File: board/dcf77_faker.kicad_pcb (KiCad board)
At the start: 4 copper layers, 69 x 32 mm, 46 parts, among them J1 Barrel_Jack, J2 DBG, J3 ANT, J4 LCD_I2C, SW1 RST, U1 NCP1117ST33T3G, U2 ATSAML21G18B-AUT, X1 32.768kHz, X2 31MHz

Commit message: board: align schematic to grid
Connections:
- U2 pad 2: /XOUT32 -> unconnected-(U2-Pad2)
- U2 pad 24: /XOUT -> unconnected-(U2-Pad24)

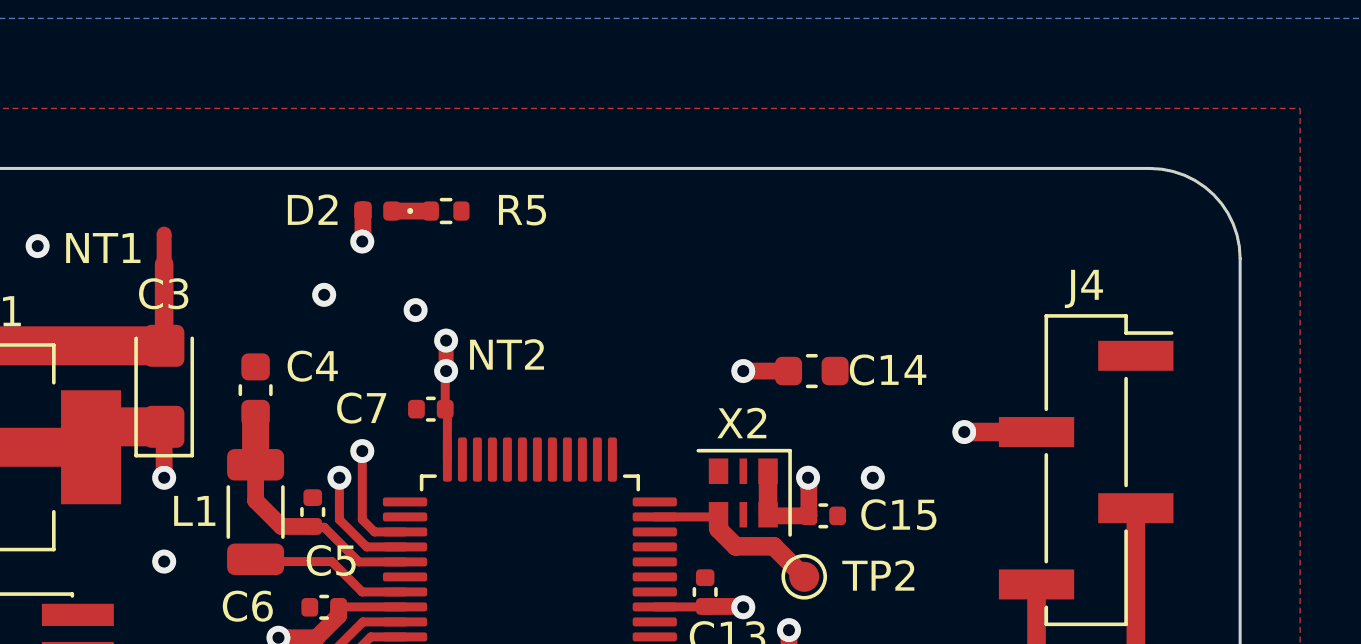
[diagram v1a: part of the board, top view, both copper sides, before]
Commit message: board: add buttons to set hour/minute or reset second
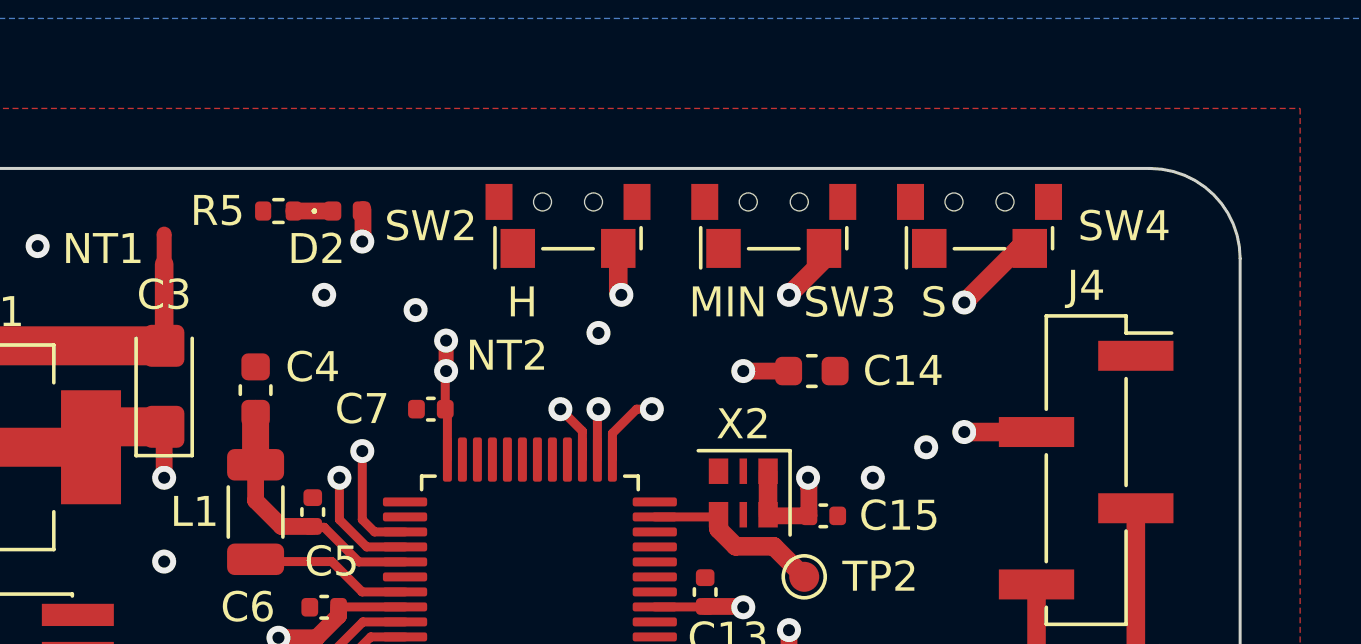
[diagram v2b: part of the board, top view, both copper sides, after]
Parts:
- added SW2: H, Button_Switch_SMD_Side:Shou_Han_TS24CA, F.Cu at (196.6, 58.2)
- added SW3: MIN, Button_Switch_SMD_Side:Shou_Han_TS24CA, F.Cu at (203.5, 58.2)
- added SW4: S, Button_Switch_SMD_Side:Shou_Han_TS24CA, F.Cu at (210.3, 58.2)
- SW1: footprint Button_Switch_SMD_Custom:Shou_Han_TS24CA -> Button_Switch_SMD_Side:Shou_Han_TS24CA
- moved R5 5.59 mm to (186.9, 58.4), turned to 0 degrees
- moved D2 1.02 mm to (189.2, 58.4), turned to 0 degrees
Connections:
- net /VDDIO1 renamed /VDDIO2
- U2 pad 25: unconnected-(U2-Pad25) -> /H
- U2 pad 26: unconnected-(U2-Pad26) -> /MIN
- U2 pad 27: unconnected-(U2-Pad27) -> /S
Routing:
- net /S: track 0.00 -> 23.3 mm, vias 0 -> 3
- net /MIN: track 0.00 -> 13.1 mm, vias 0 -> 3
- net /H: track 0.00 -> 8.34 mm, vias 0 -> 2

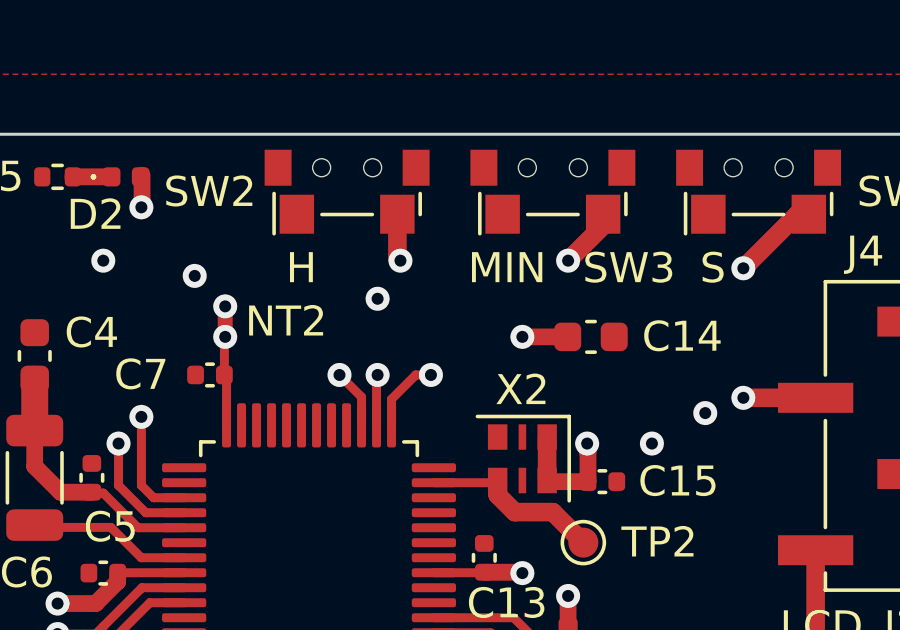
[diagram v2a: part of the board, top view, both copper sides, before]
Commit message: board: reorder HMS button pins
this increases planarity of the PCB tracks
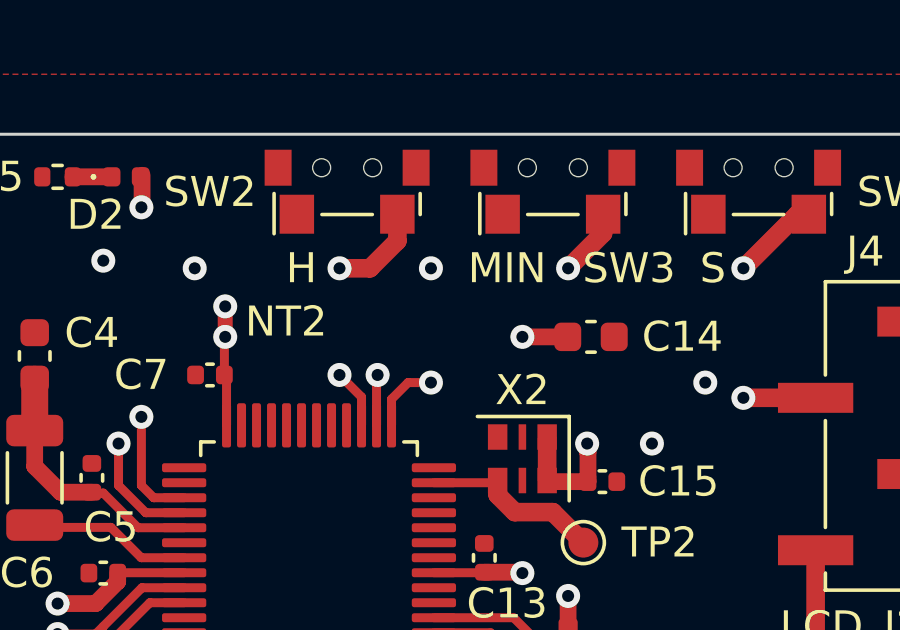
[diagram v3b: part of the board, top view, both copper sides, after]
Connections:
- U2 pad 25: /H -> /S
- U2 pad 27: /S -> /H
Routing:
- net /S: track 23.3 -> 18.6 mm
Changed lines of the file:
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@@
   (net 19 "unconnected-(J2-Pad8)")
   (net 20 "unconnected-(J2-Pad9)")
-  (net 21 "Net-(R4-Pad1)")
-  (net 22 "Net-(SW1-Pad2)")
+  (net 21 "Net-(J3-Pad1)")
+  (net 22 "Net-(R2-Pad2)")
   (net 23 "/TCC0WO0")
   (net 24 "/XIN")
@@
       (net 1 "GND") (pinfunction "1") (pintype "passive"))
     (pad "2" smd rect (at 1.675 1.5 180) (size 1.15 1.3) (layers "F.Cu" "F.Paste" "F.Mask")
-      (net 22 "Net-(SW1-Pad2)") (pinfunction "2") (pintype "passive"))
+      (net 22 "Net-(R2-Pad2)") (pinfunction "2") (pintype "passive"))
     (pad "3" smd rect (at 2.3 -0.05 180) (size 0.9 1.2) (layers "F.Cu" "F.Paste" "F.Mask"))
     (pad "3" smd rect (at -2.3 -0.05 180) (size 0.9 1.2) (layers "F.Cu" "F.Paste" "F.Mask"))
@@
       (net 10 "/~{RST}") (pintype "passive"))
     (pad "2" smd roundrect (at 0.51 0 270) (size 0.54 0.64) (layers "F.Cu" "F.Paste" "F.Mask") (roundrect_rratio 0.25)
-      (net 22 "Net-(SW1-Pad2)") (pintype "passive"))
+      (net 22 "Net-(R2-Pad2)") (pintype "passive"))
     (model "${KICAD6_3DMODEL_DIR}/Resistor_SMD.3dshapes/R_0402_1005Metric.wrl"
       (offset (xyz 0 0 0))
@@
       (net 38 "unconnected-(U2-Pad24)") (pinfunction "PA15") (pintype "bidirectional+no_connect"))
     (pad "25" smd roundrect (at 4.1625 2.75 90) (size 1.475 0.3) (layers "F.Cu" "F.Paste" "F.Mask") (roundrect_rratio 0.25)
-      (net 51 "/H") (pinfunction "PA16") (pintype "bidirectional"))
+      (net 53 "/S") (pinfunction "PA16") (pintype "bidirectional"))
     (pad "26" smd roundrect (at 4.1625 2.25 90) (size 1.475 0.3) (layers "F.Cu" "F.Paste" "F.Mask") (roundrect_rratio 0.25)
       (net 52 "/MIN") (pinfunction "PA17") (pintype "bidirectional"))
     (pad "27" smd roundrect (at 4.1625 1.75 90) (size 1.475 0.3) (layers "F.Cu" "F.Paste" "F.Mask") (roundrect_rratio 0.25)
-      (net 53 "/S") (pinfunction "PA18") (pintype "bidirectional"))
+      (net 51 "/H") (pinfunction "PA18") (pintype "bidirectional"))
     (pad "28" smd roundrect (at 4.1625 1.25 90) (size 1.475 0.3) (layers "F.Cu" "F.Paste" "F.Mask") (roundrect_rratio 0.25)
       (net 39 "unconnected-(U2-Pad28)") (pinfunction "PA19") (pintype "bidirectional+no_connect"))
@@
     (fp_line (start -0.525 0.27) (end -0.525 -0.27) (layer "F.Fab") (width 0.1))
     (pad "1" smd roundrect (at -0.51 0) (size 0.54 0.64) (layers "F.Cu" "F.Paste" "F.Mask") (roundrect_rratio 0.25)
-      (net 21 "Net-(R4-Pad1)") (pintype "passive"))
+      (net 21 "Net-(J3-Pad1)") (pintype "passive"))
     (pad "2" smd roundrect (at 0.51 0) (size 0.54 0.64) (layers "F.Cu" "F.Paste" "F.Mask") (roundrect_rratio 0.25)
       (net 23 "/TCC0WO0") (pintype "passive"))
@@
     (fp_line (start -2.54 1.59) (end -1.27 1.59) (layer "F.Fab") (width 0.1))
     (pad "1" smd rect (at 1.655 -1.27 270) (size 2.51 1) (layers "F.Cu" "F.Paste" "F.Mask")
-      (net 21 "Net-(R4-Pad1)") (pinfunction "Pin_1") (pintype "passive"))
+      (net 21 "Net-(J3-Pad1)") (pinfunction "Pin_1") (pintype "passive"))
     (pad "2" smd rect (at -1.655 1.27 270) (size 2.51 1) (layers "F.Cu" "F.Paste" "F.Mask")
       (net 1 "GND") (pinfunction "Pin_2") (pintype "passive"))
@@
   (segment (start 196.215 77.089) (end 197.104 77.978) (width 0.620014) (layer "F.Cu") (net 1))
   (segment (start 193.767 77.034) (end 193.857 77.034) (width 0.299974) (layer "F.Cu") (net 1))
-  (via (at 191.516 61.722) (size 0.8) (drill 0.4) (layers "F.Cu" "B.Cu") (free) (net 1))
+  (via (at 191.516 61.468) (size 0.8) (drill 0.4) (layers "F.Cu" "B.Cu") (free) (net 1))
   (via (at 178.9176 59.5884) (size 0.8) (drill 0.4) (layers "F.Cu" "B.Cu") (free) (net 1))
   (via (at 206.756 67.31) (size 0.8) (drill 0.4) (layers "F.Cu" "B.Cu") (free) (net 1))
@@
   (segment (start 187.452 72.644) (end 188.214 73.406) (width 0.620014) (layer "In1.Cu") (net 48))
   (segment (start 200.152 82.55) (end 188.214 82.55) (width 0.620014) (layer "In2.Cu") (net 48))
-  (segment (start 198.076 65.83) (end 198.882 65.024) (width 0.299974) (layer "F.Cu") (net 51))
-  (segment (start 198.076 66.7035) (end 198.076 65.83) (width 0.299974) (layer "F.Cu") (net 51))
-  (segment (start 198.271 61.111) (end 198.374 61.214) (width 0.620014) (layer "F.Cu") (net 51))
-  (segment (start 198.271 59.666) (end 198.271 61.111) (width 0.620014) (layer "F.Cu") (net 51))
-  (segment (start 198.882 65.024) (end 199.39 65.024) (width 0.299974) (layer "F.Cu") (net 51))
-  (via (at 198.374 61.214) (size 0.8) (drill 0.4) (layers "F.Cu" "B.Cu") (net 51))
-  (via (at 199.39 65.024) (size 0.8) (drill 0.4) (layers "F.Cu" "B.Cu") (net 51))
-  (segment (start 199.39 65.024) (end 199.39 62.23) (width 0.56007) (layer "In1.Cu") (net 51))
-  (segment (start 199.39 62.23) (end 198.374 61.214) (width 0.56007) (layer "In1.Cu") (net 51))
-  (segment (start 205.129 59.666) (end 205.129 60.047) (width 0.620014) (layer "F.Cu") (net 52))
+  (segment (start 198.271 59.666) (end 198.271 60.555) (width 0.620014) (layer "F.Cu") (net 51))
+  (segment (start 197.076 66.7035) (end 197.076 65.758) (width 0.299974) (layer "F.Cu") (net 51))
+  (segment (start 197.076 65.758) (end 196.342 65.024) (width 0.299974) (layer "F.Cu") (net 51))
+  (segment (start 198.271 60.555) (end 197.358 61.468) (width 0.620014) (layer "F.Cu") (net 51))
+  (segment (start 197.358 61.468) (end 196.342 61.468) (width 0.620014) (layer "F.Cu") (net 51))
+  (via (at 196.342 65.024) (size 0.8) (drill 0.4) (layers "F.Cu" "B.Cu") (net 51))
+  (via (at 196.342 61.468) (size 0.8) (drill 0.4) (layers "F.Cu" "B.Cu") (net 51))
+  (segment (start 196.342 65.024) (end 196.342 61.468) (width 0.620014) (layer "In1.Cu") (net 51))
+  (segment (start 205.129 59.666) (end 205.129 60.301) (width 0.620014) (layer "F.Cu") (net 52))
   (segment (start 197.576 65.06) (end 197.612 65.024) (width 0.299974) (layer "F.Cu") (net 52))
   (segment (start 197.576 66.7035) (end 197.576 65.06) (width 0.299974) (layer "F.Cu") (net 52))
-  (segment (start 205.129 60.047) (end 203.962 61.214) (width 0.620014) (layer "F.Cu") (net 52))
-  (via (at 203.962 61.214) (size 0.8) (drill 0.4) (layers "F.Cu" "B.Cu") (net 52))
-  (via (at 197.612 62.484) (size 0.8) (drill 0.4) (layers "F.Cu" "B.Cu") (net 52))
+  (segment (start 205.129 60.301) (end 203.962 61.468) (width 0.620014) (layer "F.Cu") (net 52))
+  (via (at 203.962 61.468) (size 0.8) (drill 0.4) (layers "F.Cu" "B.Cu") (net 52))
+  (via (at 199.39 61.468) (size 0.8) (drill 0.4) (layers "F.Cu" "B.Cu") (net 52))
   (via (at 197.612 65.024) (size 0.8) (drill 0.4) (layers "F.Cu" "B.Cu") (net 52))
-  (segment (start 197.612 65.024) (end 197.612 62.484) (width 0.56007) (layer "In1.Cu") (net 52))
-  (segment (start 197.612 62.484) (end 202.692 62.484) (width 0.56007) (layer "In2.Cu") (net 52))
-  (segment (start 202.692 62.484) (end 203.962 61.214) (width 0.56007) (layer "In2.Cu") (net 52))
+  (segment (start 197.612 65.024) (end 197.612 63.246) (width 0.620014) (layer "In1.Cu") (net 52))
+  (segment (start 197.612 63.246) (end 199.39 61.468) (width 0.620014) (layer "In1.Cu") (net 52))
+  (segment (start 199.39 61.468) (end 203.962 61.468) (width 0.620014) (layer "In2.Cu") (net 52))
   (segment (start 211.606 59.666) (end 209.804 61.468) (width 0.620014) (layer "F.Cu") (net 53))
   (segment (start 211.987 59.666) (end 211.606 59.666) (width 0.620014) (layer "F.Cu") (net 53))
-  (segment (start 197.076 66.7035) (end 197.076 65.758) (width 0.299974) (layer "F.Cu") (net 53))
-  (segment (start 197.076 65.758) (end 196.342 65.024) (width 0.299974) (layer "F.Cu") (net 53))
-  (via (at 208.534 66.294) (size 0.8) (drill 0.4) (layers "F.Cu" "B.Cu") (net 53))
-  (via (at 196.342 65.024) (size 0.8) (drill 0.4) (layers "F.Cu" "B.Cu") (net 53))
+  (segment (start 198.076 66.7035) (end 198.076 65.83) (width 0.299974) (layer "F.Cu") (net 53))
+  (segment (start 198.076 65.83) (end 198.628 65.278) (width 0.299974) (layer "F.Cu") (net 53))
+  (segment (start 198.628 65.278) (end 199.39 65.278) (width 0.299974) (layer "F.Cu") (net 53))
+  (via (at 208.534 65.278) (size 0.8) (drill 0.4) (layers "F.Cu" "B.Cu") (net 53))
+  (via (at 199.39 65.278) (size 0.8) (drill 0.4) (layers "F.Cu" "B.Cu") (net 53))
   (via (at 209.804 61.468) (size 0.8) (drill 0.4) (layers "F.Cu" "B.Cu") (net 53))
-  (segment (start 208.534 66.294) (end 208.534 62.738) (width 0.620014) (layer "In1.Cu") (net 53))
   (segment (start 208.534 62.738) (end 209.804 61.468) (width 0.620014) (layer "In1.Cu") (net 53))
-  (segment (start 196.342 65.024) (end 196.342 65.532) (width 0.56007) (layer "In2.Cu") (net 53))
-  (segment (start 196.342 65.532) (end 197.104 66.294) (width 0.56007) (layer "In2.Cu") (net 53))
-  (segment (start 197.104 66.294) (end 208.534 66.294) (width 0.56007) (layer "In2.Cu") (net 53))
+  (segment (start 208.534 62.738) (end 208.534 65.024) (width 0.620014) (layer "In1.Cu") (net 53))
+  (segment (start 199.39 65.278) (end 208.534 65.278) (width 0.620014) (layer "In2.Cu") (net 53))
   (segment (start 199.4885 71.616) (end 201.156 71.616) (width 0.299974) (layer "F.Cu") (net 54))
   (segment (start 192.504 65.024) (end 192.504 63.782) (width 0.299974) (layer "F.Cu") (net 54))

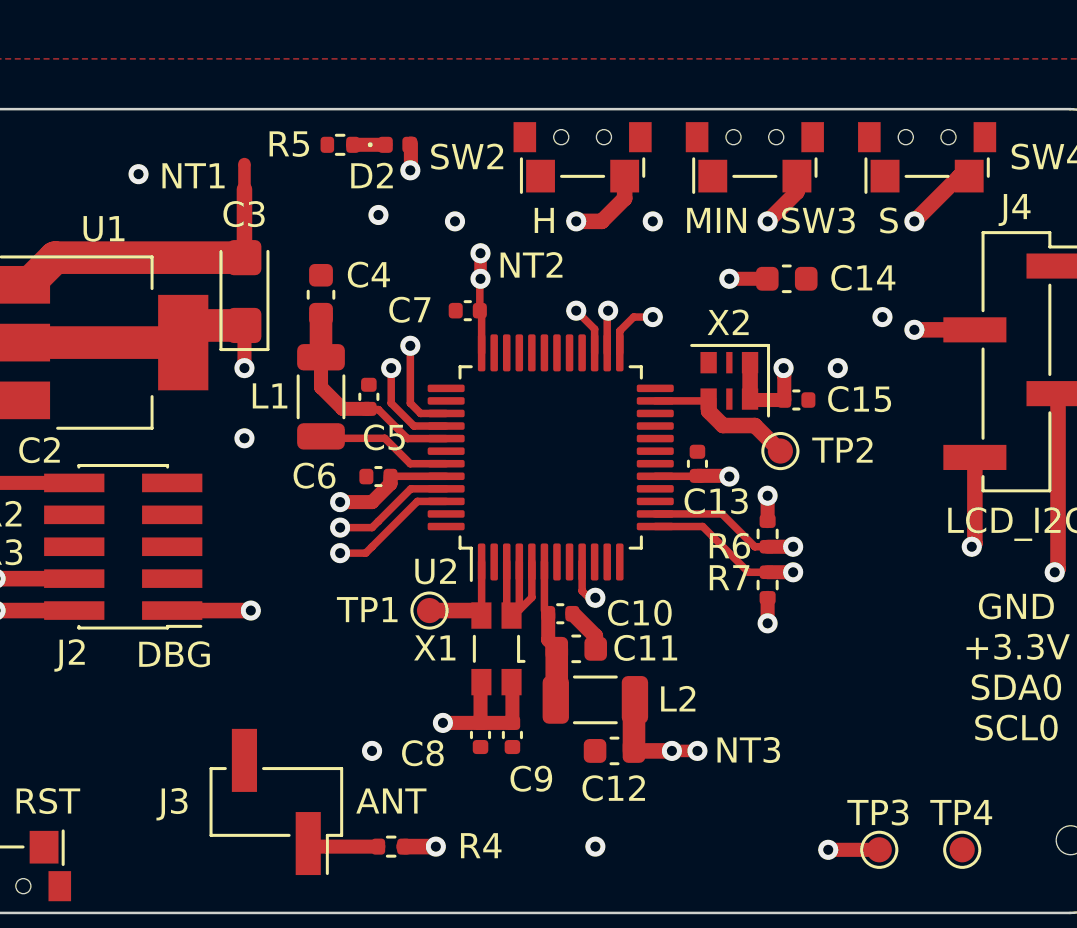
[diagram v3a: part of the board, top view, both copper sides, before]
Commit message: board: force VDDIO1 and VDDIO2 to be independent nets
otherwise the name of the common net will keep changing
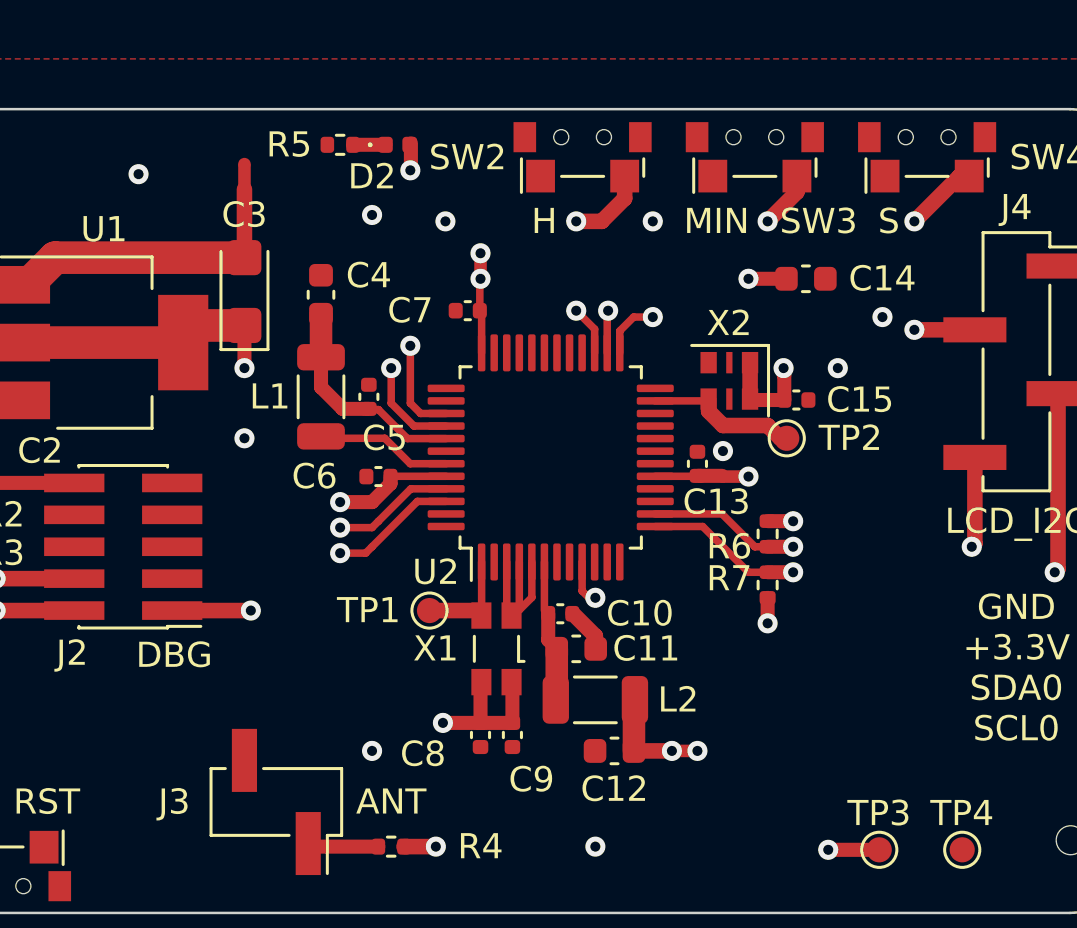
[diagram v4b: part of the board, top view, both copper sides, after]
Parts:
- added NT4: NetTie_2, NetTie:NetTie-2_SMD_Pad0.5mm, F.Cu at (202.7, 71.6)
- moved C14 0.76 mm to (205.5, 63.8)
- moved TP2 0.57 mm to (204.7, 70.1)
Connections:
- C13 pad 1: /VDDIO2 -> /VDDIO1
- U2 pad 17: /VDDIO2 -> /VDDIO1
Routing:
- net /VDDIO1: track 0.00 -> 2.66 mm
- net /VDDIO2: track 25.2 -> 23.0 mm
- net GND: vias 4 -> 5
